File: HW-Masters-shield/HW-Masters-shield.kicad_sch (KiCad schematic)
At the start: 22 parts, among them J1 12V, J2 Bornera 2, J3 Salida de relevador, J4 Bornera 1, K1 G5LE-1, Q1 ntr4003nt1g O AO 3400

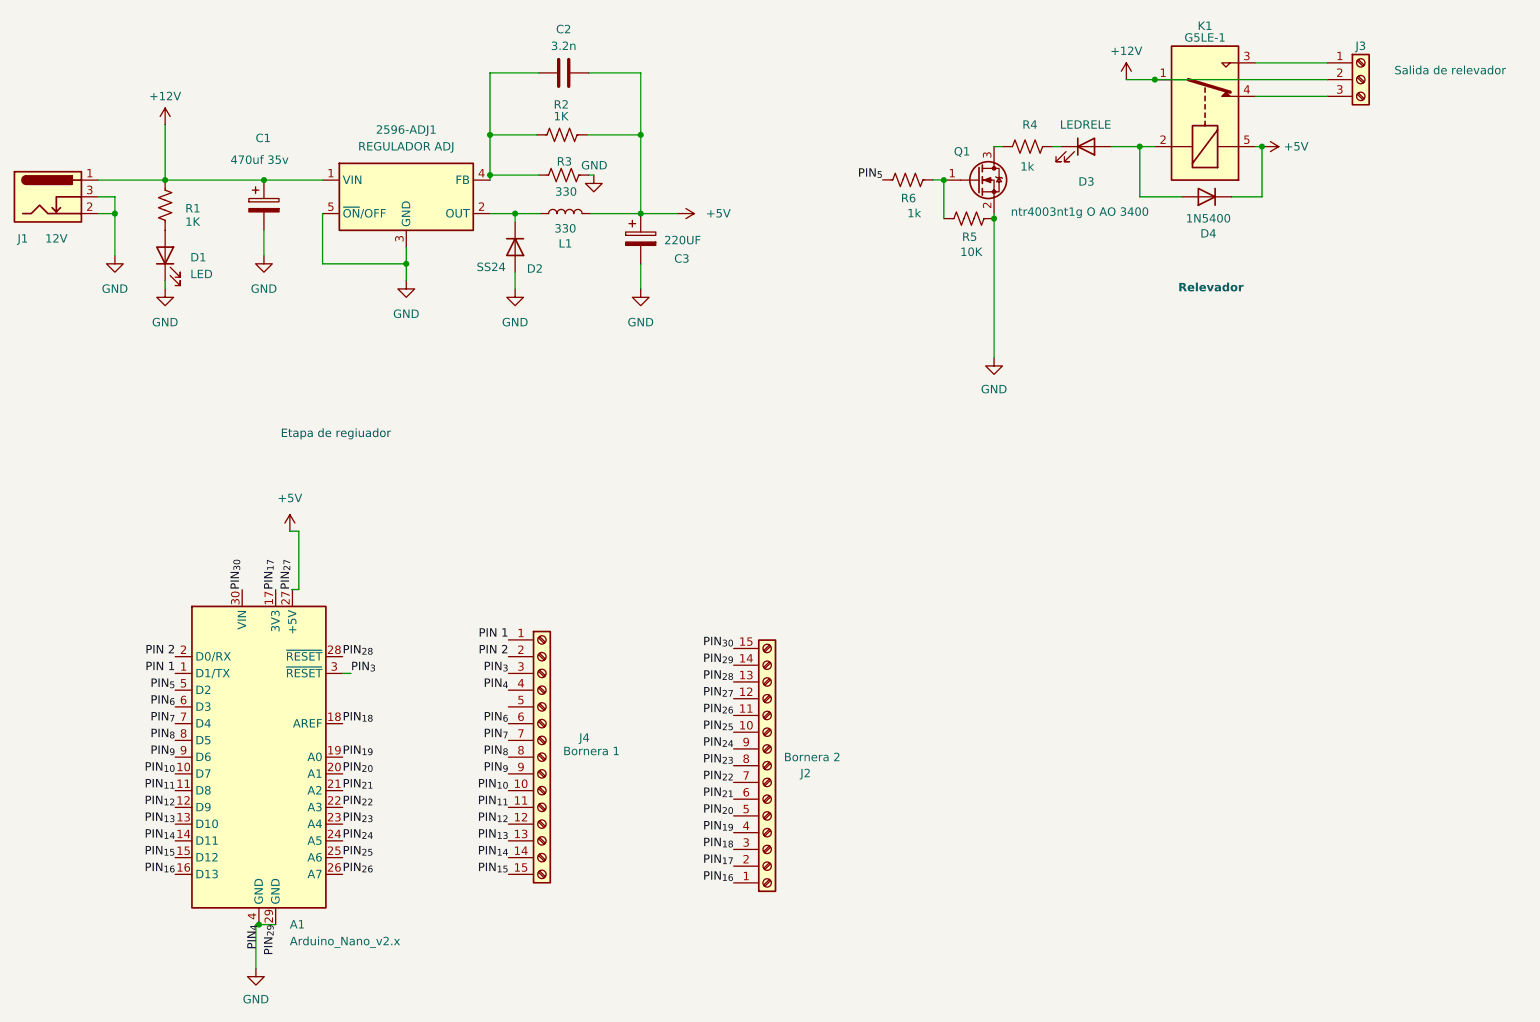
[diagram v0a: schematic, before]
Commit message: FEAT: crrijo error de mosfet y de falta de berreno de montaje
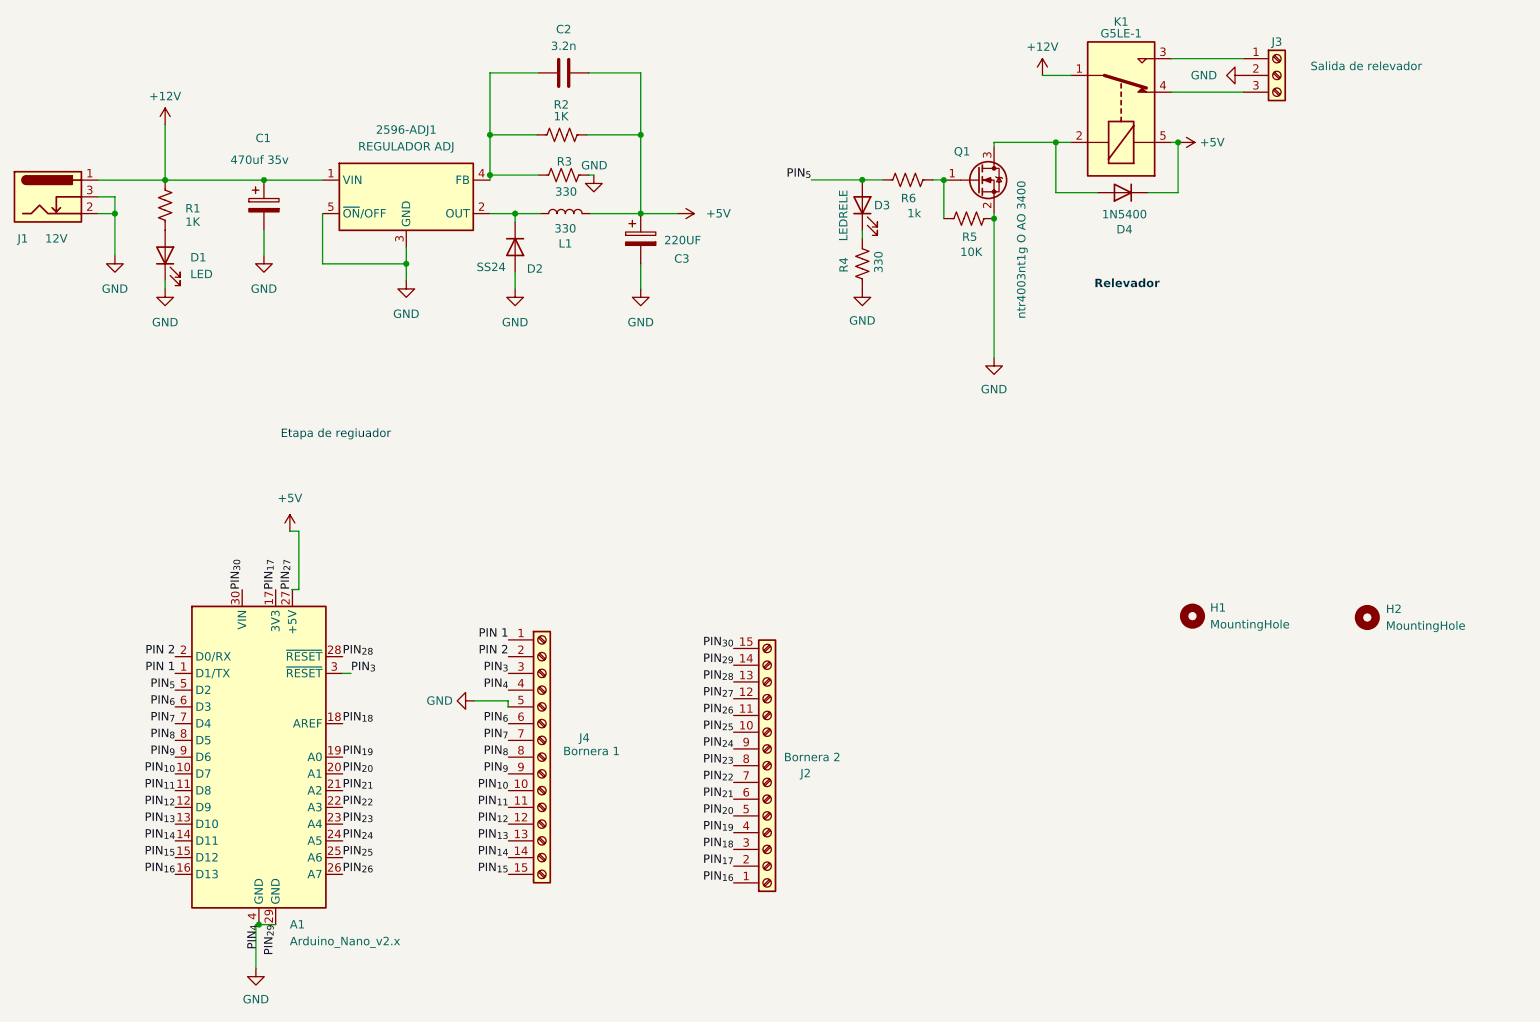
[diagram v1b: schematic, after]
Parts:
- added H1, H2: MountingHole, MountingHole:MountingHole_3.2mm_M3_Pad_Via, symbol Mechanical:MountingHole
- J2, J4: footprint TerminalBlock_Phoenix:TerminalBlock_Phoenix_MKDS-3-15-5.08_1x15_P5.08mm_Horizontal -> TerminalBlock_Altech:Altech_AK100_1x15_P5.00mm
- J3: footprint TerminalBlock_Phoenix:TerminalBlock_Phoenix_MKDS-3-3-5.08_1x03_P5.08mm_Horizontal -> TerminalBlock_Altech:Altech_AK100_1x03_P5.00mm
- R4: value 1k -> 330
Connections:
- net +12V: no longer J3.2 (Pin_2)
- net GND: now also J3.2 (Pin_2), J4.5 (Pin_5), R4.1
- net PIN_{5}: now also D3.2 (A)
- net at Q1.3 (D): now also D4.2 (A), K1.2; no longer R4.1
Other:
- moved on the sheet: D3, D4, J3, K1, R4
